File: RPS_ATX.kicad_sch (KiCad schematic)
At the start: 35 parts, among them J1 494_ON, J10 MCU_FAN, J11 PW_IN, J13 FAN_OUT, J5 PS_OUT-, J6 PS_OUT+, J7 RPS_OUT-, J8 MEAS, J9 RPS_OUT+, Q3 AO3400A, U2 Mini360, U4 TL431DBZ, U5 LM358, U6 INA226, U7 LM7805_TO220

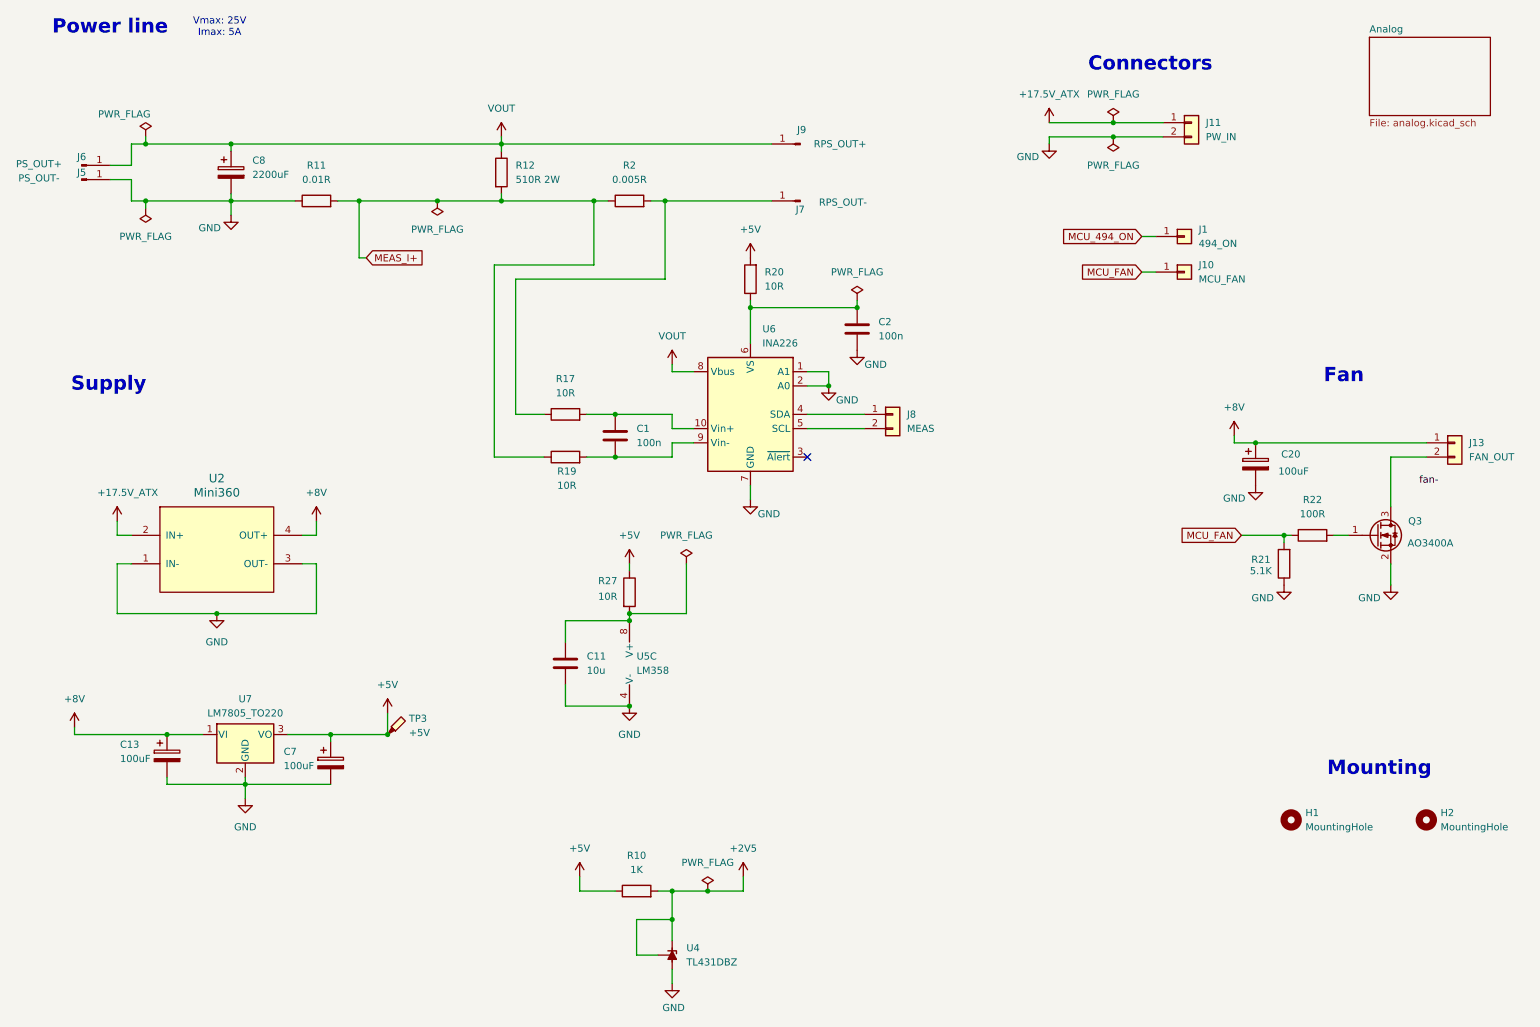
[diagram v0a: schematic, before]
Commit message: added: fuse(+17V), C(+17V) , INA226 pullup resistors
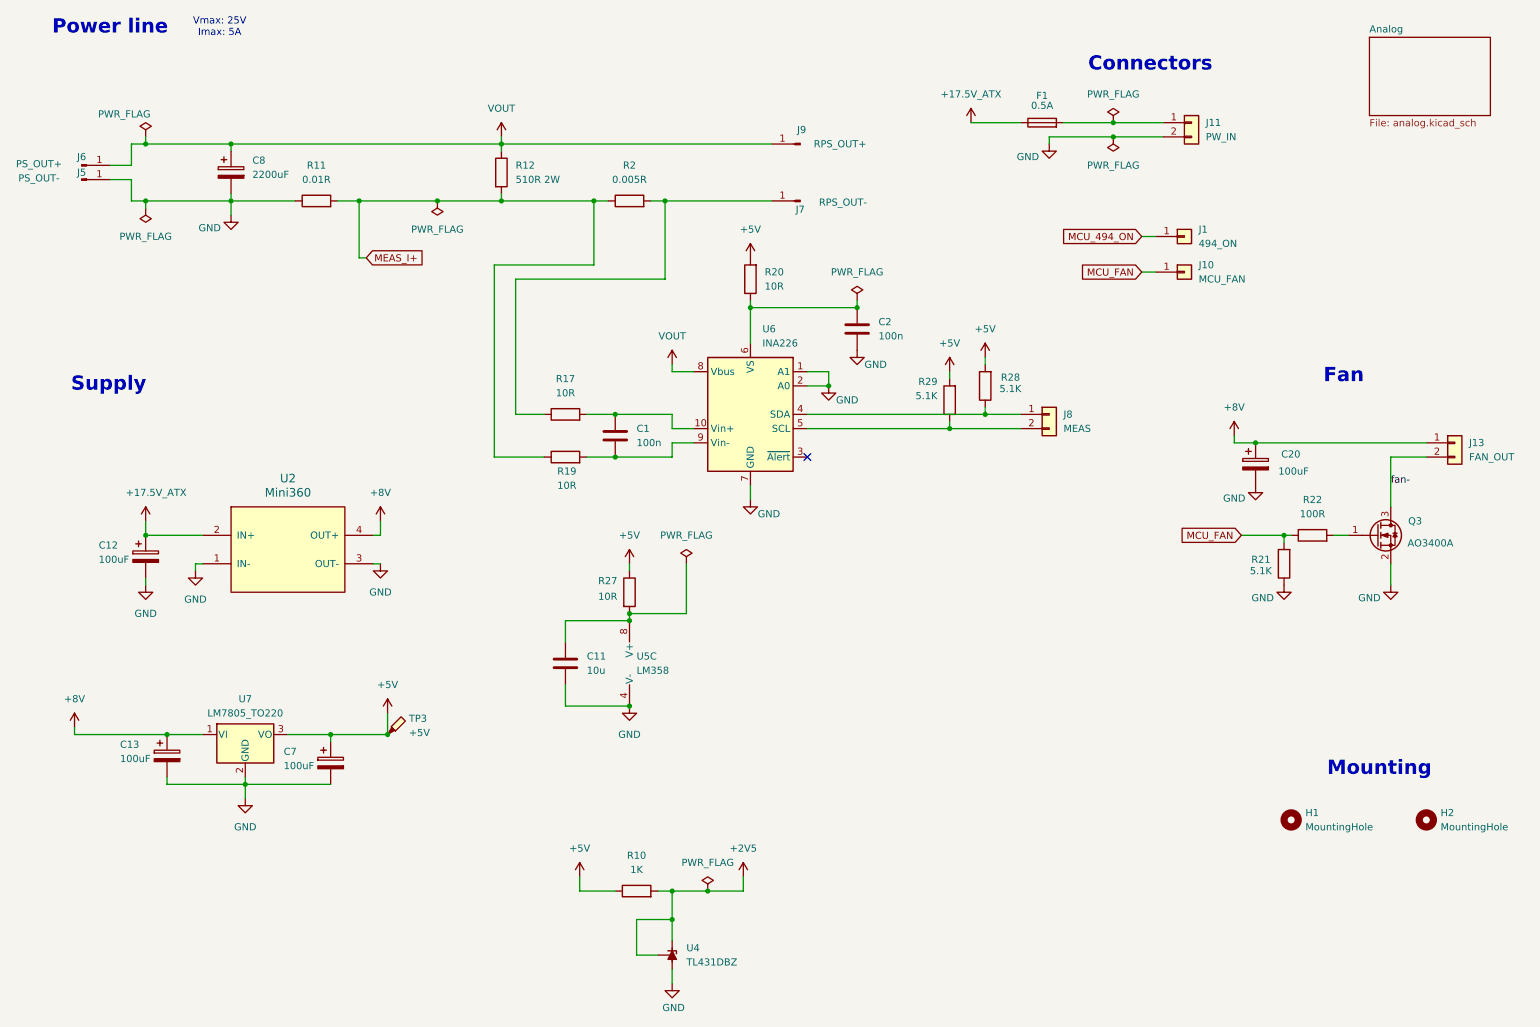
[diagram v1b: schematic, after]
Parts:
- added C12: 100uF, Capacitor_SMD:CP_Elec_6.3x5.4_Nichicon, symbol Device:C_Polarized
- added F1: 0.5A, Fuse:Fuse_1206_3216Metric_Pad1.42x1.75mm_HandSolder, symbol Device:Fuse
- added R28, R29: 5.1K, Resistor_SMD:R_0805_2012Metric_Pad1.20x1.40mm_HandSolder, symbol Device:R
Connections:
- net +17.5V_ATX: now also C12.1, F1.1; no longer J11.1 (Pin_1)
- net +5V: now also R28.2, R29.2
- net GND: now also C12.2
- net fan-: now also J13.2 (Pin_2), Q3.3 (D)
- net at J8.1 (Pin_1), U6.4 (SDA): now also R28.1
- net at J8.2 (Pin_2), U6.5 (SCL): now also R29.1
- new net: F1.2, J11.1 (Pin_1)
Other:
- moved on the sheet: J8, U2

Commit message: ref voltage from 2.5 to 5 V
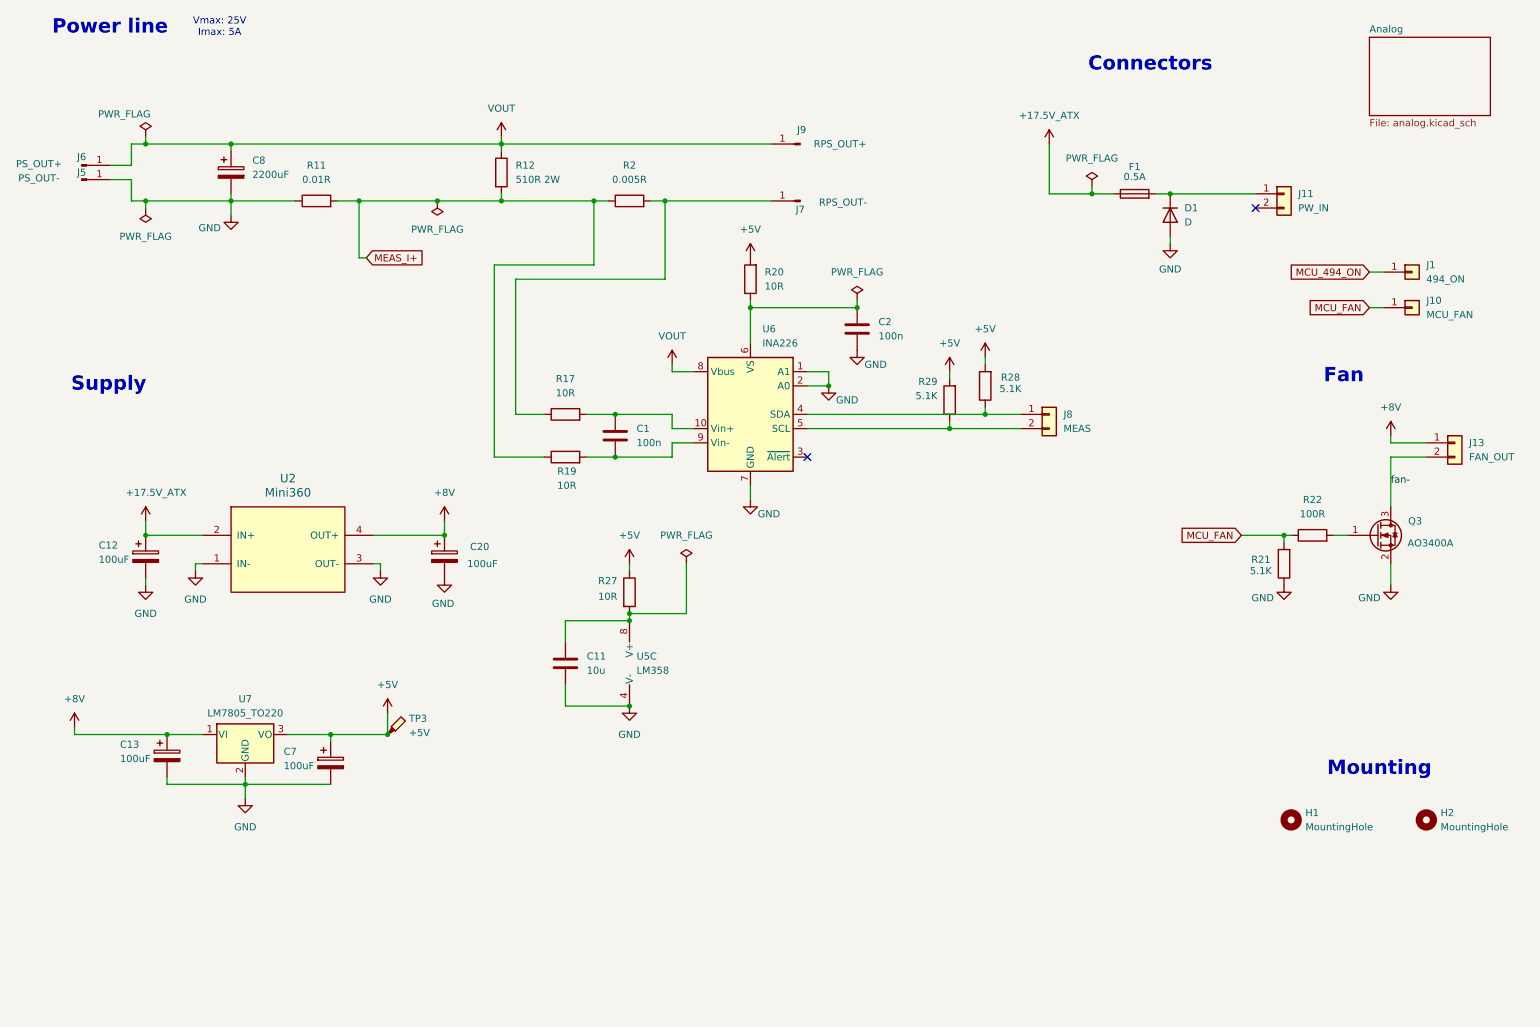
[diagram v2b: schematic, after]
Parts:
- removed R10: 1K, Resistor_SMD:R_1206_3216Metric_Pad1.30x1.75mm_HandSolder, symbol Device:R
- removed U4: TL431DBZ, Package_TO_SOT_SMD:SOT-23, symbol Reference_Voltage:TL431DBZ
- added D1: D, Diode_SMD:D_1206_3216Metric_Pad1.42x1.75mm_HandSolder, symbol Device:D
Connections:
- net GND: now also D1.2 (A); no longer J11.2 (Pin_2)
- net at F1.2, J11.1 (Pin_1): now also D1.1 (K)
- no-connect marks 1 -> 2
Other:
- moved on the sheet: C20, F1, J1, J10, J11

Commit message: +5Vref for softstart, power LED,another connectors
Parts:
- removed J11: PW_IN, Connector_PinHeader_2.54mm:PinHeader_1x02_P2.54mm_Vertical, symbol Connector_Generic:Conn_01x02
- removed J8: MEAS, Connector_PinHeader_2.54mm:PinHeader_1x02_P2.54mm_Vertical, symbol Connector_Generic:Conn_01x02
- added D2: PW_LED, LED_SMD:LED_1206_3216Metric_Pad1.42x1.75mm_HandSolder, symbol Device:LED
- added J4: MCU, Connector_PinHeader_2.54mm:PinHeader_1x04_P2.54mm_Vertical, symbol Connector_Generic:Conn_01x04
- added R10: 1K, Resistor_SMD:R_1206_3216Metric_Pad1.30x1.75mm_HandSolder, symbol Device:R
- F1: value 0.5A -> 1A
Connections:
- net +5V: now also D2.2 (A), J4.3 (Pin_3); no longer R27.1
- net GND: now also J4.4 (Pin_4), R10.2
- net at R28.1, U6.4 (SDA): now also J4.1 (Pin_1)
- net at R29.1, U6.5 (SCL): now also J4.2 (Pin_2)
- net +17.5V: now reaches D1.1 (K), F1.2
- net +8V renamed +12V
- net +12V: now also R27.1
- new net: D2.1 (K), R10.1
- no-connect marks 2 -> 1
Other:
- note added: "Optional"
- moved on the sheet: H1, H2, J13, Q3, R21, R22, TP3
